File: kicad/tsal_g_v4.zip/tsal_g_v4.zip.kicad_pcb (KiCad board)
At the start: 2 copper layers, 115 x 60 mm, 92 parts, among them J1 Conn_01x02_Pin, J2 Conn_01x02_Pin, J3 Conn_01x06_Pin, J6 Conn_01x02_Pin, J7 Conn_01x02_Pin, J8 Conn_01x03, Q1 2N7002, Q2 NCE60P04R, U1 TL431DBZ, U10 BU4S01G2, U11 BU4S01G2, U14 BUS4S71G2, U15 BUS4S71G2, U16 BU4SU69G2, U17 40106, U18 BU4S01G2, U19 BU4S01G2, U2 LTV-817S, U20 4071, U3 B1212, U4 BU4SU69G2, U5 40106, U6 40106, U7 BU4S81G2

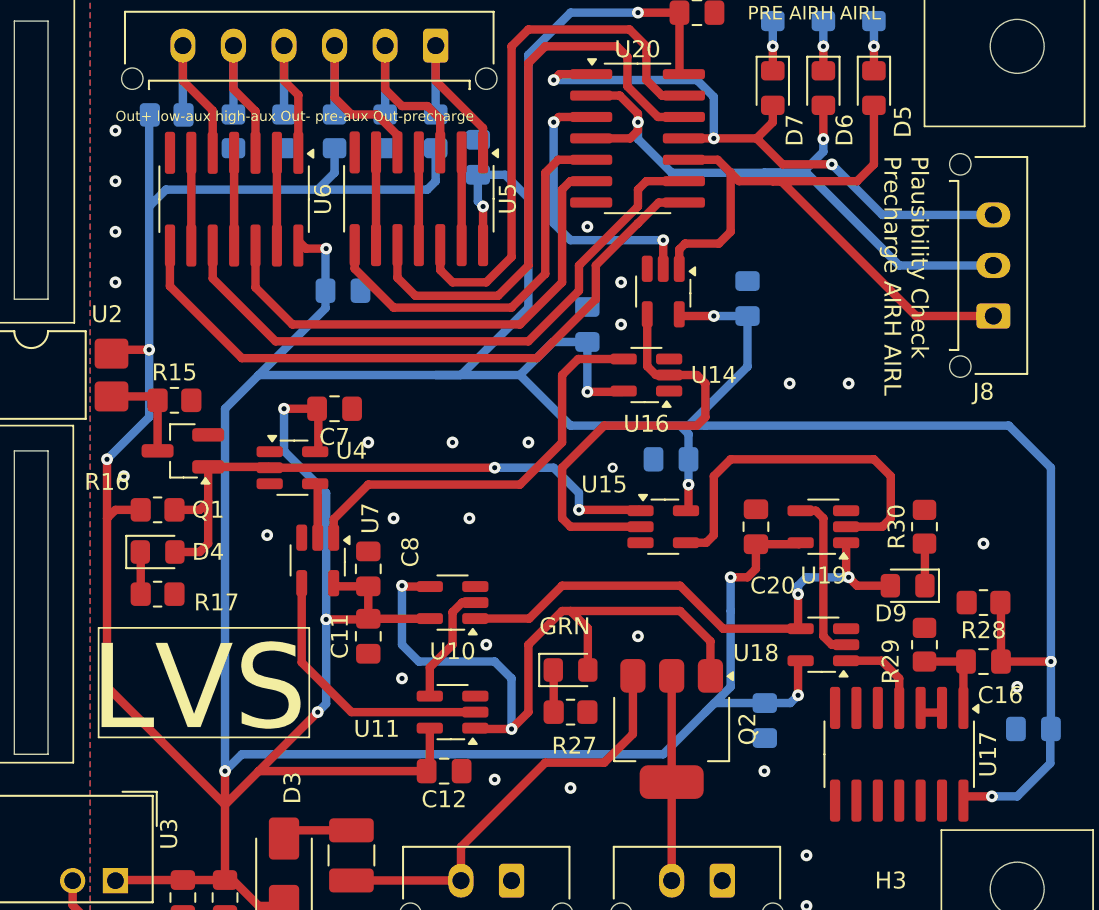
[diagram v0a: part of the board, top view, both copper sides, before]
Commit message: changed tsal_g traces
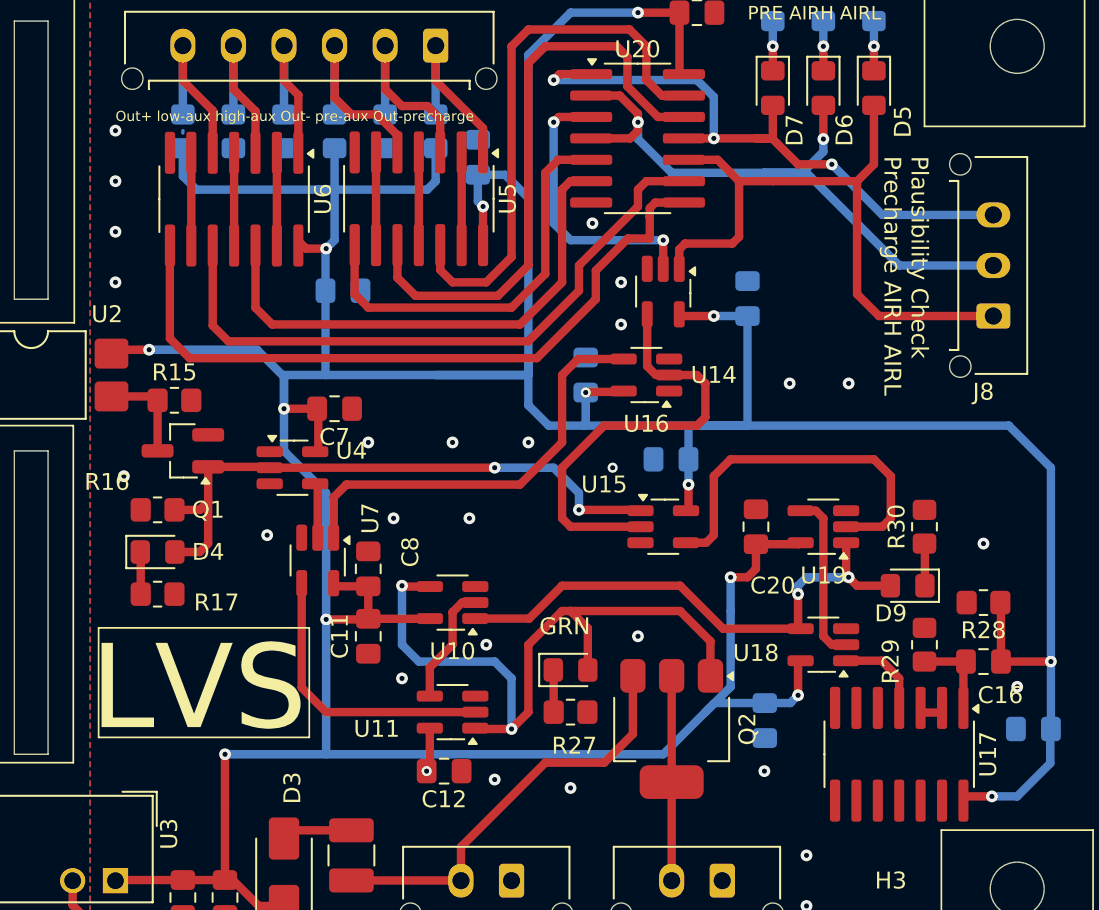
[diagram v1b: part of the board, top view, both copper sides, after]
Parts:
- moved C18 3.00 mm to (140.9, 77.5)
- moved R22 1.37 mm to (117.0, 63.0), turned to -90 degrees
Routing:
- net VCC: track 381.1 -> 309.9 mm, vias 16 -> 15
- net Out +: track 39.7 -> 42.4 mm
- net low aux: track 36.9 -> 38.5 mm
- net AIRL Check: track 40.5 -> 39.6 mm
- net Out -: track 24.1 -> 25.0 mm
- net Net-(U11-Pad2): track 16.2 -> 17.1 mm
- net RELAY LOGIC: track 24.6 -> 25.3 mm
- net high aux: track 30.6 -> 31.3 mm
- net Precharge Check: track 37.9 -> 38.5 mm

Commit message: updated tsal
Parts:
- removed C20: 0.1uF, Capacitor_SMD:C_0805_2012Metric_Pad1.18x1.45mm_HandSolder
- removed D8: LED, LED_SMD:LED_0805_2012Metric_Pad1.15x1.40mm_HandSolder
- removed Q2: NCE60P04R, Package_TO_SOT_SMD:SOT-223-3_TabPin2
- removed R27: 1k, Resistor_SMD:R_0805_2012Metric_Pad1.20x1.40mm_HandSolder
- removed U15: BUS4S71G2, Package_TO_SOT_SMD:SOT-23-5_HandSoldering
- removed U17: 40106, to be sorted:SOIC-14_3.9x8.7mm_P1.27mm_extendedpad
- removed U18, U19: BU4S01G2, Package_TO_SOT_SMD:SOT-23-5_HandSoldering
- added D10: LED, RMC_LED:LED_0805_2012Metric_Pad1.45x1.40mm_HandSolder, F.Cu at (168.4, 82.3)
- added Q4: QM6015D, RMC_TO:TO-252-2, F.Cu at (162.4, 85.0)
- added R31: 1k, RMC_Resistor:R_0805_2012Metric_Pad1.20x1.40mm_HandSolder_L, F.Cu at (168.4, 87.1)
- added U12: 4077, RMC_SO:SOIC127P600X175-14N, F.Cu at (144.4, 89.4)
- added U13: BU4S71G2, RMC_SOT:SOT-23-5_HandSoldering_Extended_RMC, F.Cu at (144.3, 82.5)
- added U9: 40106, RMC_SO:SOIC127P600X175-14N, F.Cu at (135.1, 89.3)
- C1, C11, C12, C16, C2, C24, C3, C4, C5, C6, C7, C8, C9: footprint Capacitor_SMD:C_0805_2012Metric_Pad1.18x1.45mm_HandSolder -> RMC_Capacitor:C_0805_2012Metric_Pad1.18x1.45mm_HandSolder_L
- C15, C17, C18, C19, C21, C22, C23: footprint Capacitor_SMD:C_0805_2012Metric_Pad1.18x1.45mm_HandSolder -> RMC_Capacitor:C_0805_2012Metric_Pad1.18x1.45mm_HandSolder_L; moved to F.Cu
- D2, D4, D5, D6, D7, D9: footprint LED_SMD:LED_0805_2012Metric_Pad1.15x1.40mm_HandSolder -> RMC_LED:LED_0805_2012Metric_Pad1.45x1.40mm_HandSolder
- D3: footprint Diode_SMD:D_SMA -> Diode_SMD:D_SMA_Handsoldering
- F2: footprint Fuse:Fuse_1210_3225Metric_Pad1.42x2.65mm_HandSolder -> to be sorted:Fuse_1210_3225Metric_Pad1.42x2.65mm_HandSolder
- LM1: footprint Package_SO:SOIC-8_3.9x4.9mm_P1.27mm -> RMC_SO:SOIC-8_3.9x4.9mm_P1.27mm_RMC_Handsolder
- Q1, U1: footprint Package_TO_SOT_SMD:SOT-23_Handsoldering -> RMC_SOT:SOT-23
- R1, R10, R11, R12, R13, R14, R15, R16, R17, R2, R28, R29, R3, R30, R4, R5, R6, R7, R8, R9: footprint Resistor_SMD:R_0805_2012Metric_Pad1.20x1.40mm_HandSolder -> RMC_Resistor:R_0805_2012Metric_Pad1.20x1.40mm_HandSolder_L
- R18, R19, R20, R21, R22, R23, R24, R25, R26: footprint Resistor_SMD:R_0805_2012Metric_Pad1.20x1.40mm_HandSolder -> RMC_Resistor:R_0805_2012Metric_Pad1.20x1.40mm_HandSolder_L; moved to F.Cu
- U10, U11, U14, U16, U7: footprint Package_TO_SOT_SMD:SOT-23-5_HandSoldering -> RMC_SOT:SOT-23-5_HandSoldering_Extended_RMC
- U20, U5, U6: footprint to be sorted:SOIC-14_3.9x8.7mm_P1.27mm_extendedpad -> RMC_SO:SOIC127P600X175-14N
- moved C11 40.1 mm to (167.3, 101.2), turned to 180 degrees
- moved U10 35.7 mm to (168.0, 98.0)
- moved C23 33.7 mm to (137.3, 83.5), turned to 180 degrees
- moved C16 33.6 mm to (132.8, 83.5)
- moved R29 30.8 mm to (132.7, 81.3), turned to 0 degrees
- moved U7 29.9 mm to (153.4, 98.0), turned to 0 degrees
- moved C12 29.8 mm to (161.6, 94.8), turned to 0 degrees
- moved R28 28.9 mm to (137.3, 81.3), turned to 0 degrees
- moved U11 27.8 mm to (160.8, 98.0), turned to 0 degrees
- moved C8 26.8 mm to (154.1, 94.8), turned to 0 degrees
- moved J8 25.0 mm to (147.4, 56.3), turned to 0 degrees
- moved C18 20.2 mm to (161.0, 75.6), turned to 180 degrees
- moved C19 19.7 mm to (145.0, 79.4), turned to 180 degrees
- moved U16 18.0 mm to (161.8, 72.4), turned to 0 degrees
- moved D9 17.9 mm to (142.8, 95.2)
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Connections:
- C19 pad 1: GLV- -> VCC
- C19 pad 2: VCC -> GLV-
- U16 pad 3: GLV- -> VCC
- U16 pad 5: VCC -> GLV-
- U20 pad 1: Precharge Check -> Out -
- U20 pad 10: AIRL Check -> Net-(U14-Pad2)
- U20 pad 11: Precharge Check -> AIRL Check
- U20 pad 12: pre aux -> Out +
- U20 pad 13: Out Precharge -> low aux
- U20 pad 2: AIRH Check -> high aux
- U20 pad 3: Net-(U14-Pad2) -> AIRH Check
- U20 pad 4: AIRH Check -> Precharge Check
- U20 pad 5: Out - -> pre aux
- U20 pad 6: high aux -> Out Precharge
- U20 pad 8: Out + -> Precharge Check
- U20 pad 9: low aux -> AIRH Check
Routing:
- net VCC: track 309.9 -> 11.8 mm, vias 15 -> 0
- net AIRL Check: track 39.6 -> 4.34 mm
- net Net-(Q4-G): track 41.4 -> 7.88 mm, vias 2 -> 0
- net RESET: track 31.8 -> 0.00 mm, vias 2 -> 0
- net AIRH Check: track 38.6 -> 8.05 mm, vias 2 -> 0
- net Precharge Check: track 38.5 -> 8.28 mm, vias 3 -> 0
- net TS RESET: track 36.3 -> 6.98 mm, vias 2 -> 0
- net RELAY LOGIC: track 25.3 -> 0.00 mm
- net GLV+: track 24.9 -> 0.00 mm
- net RELAY RESET: track 26.6 -> 3.97 mm
- net Net-(U15-Pad4): track 22.0 -> 0.00 mm
- net Out Precharge: track 32.6 -> 14.2 mm, vias 0 -> 2
- net pre aux: track 35.3 -> 18.8 mm, vias 0 -> 2
- net Net-(U14-Pad2): track 17.2 -> 4.20 mm, vias 2 -> 0
- net Net-(U11-Pad2): track 17.1 -> 4.53 mm
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
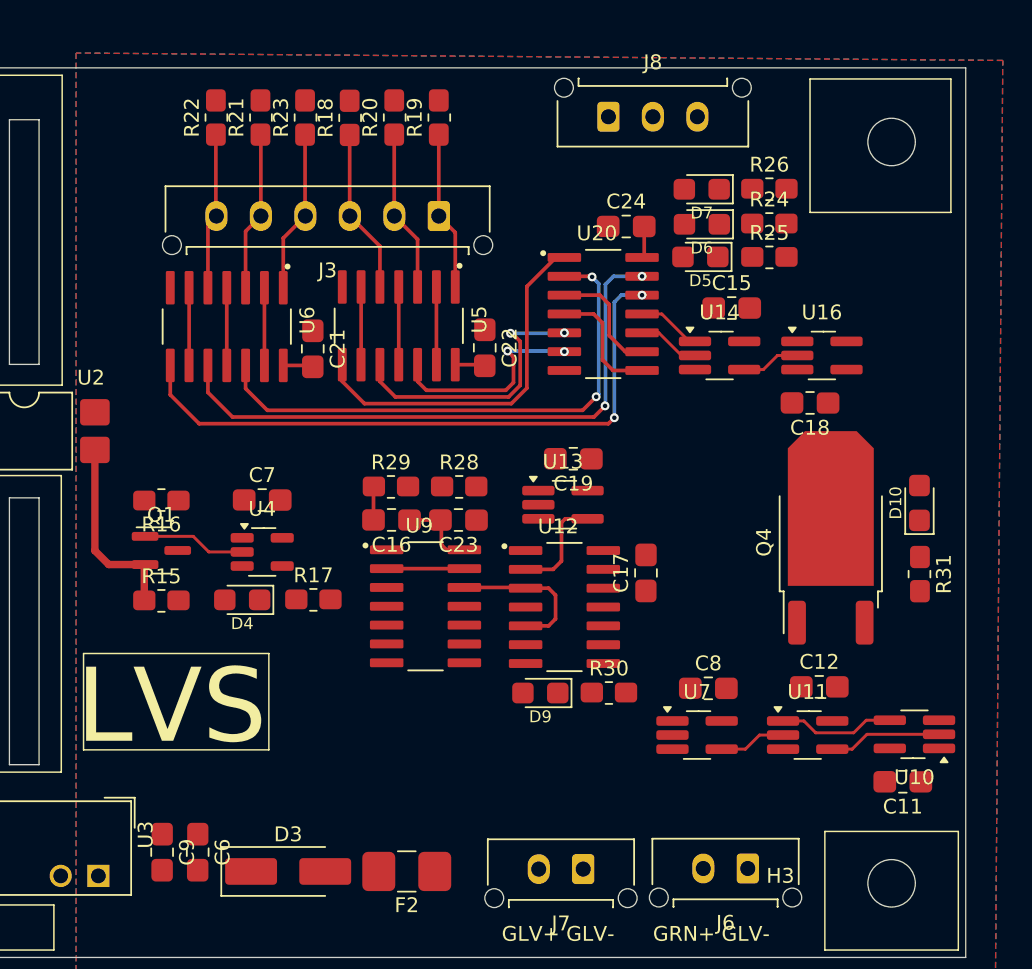
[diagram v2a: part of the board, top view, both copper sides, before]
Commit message: updated layout of tsal, need final touhces
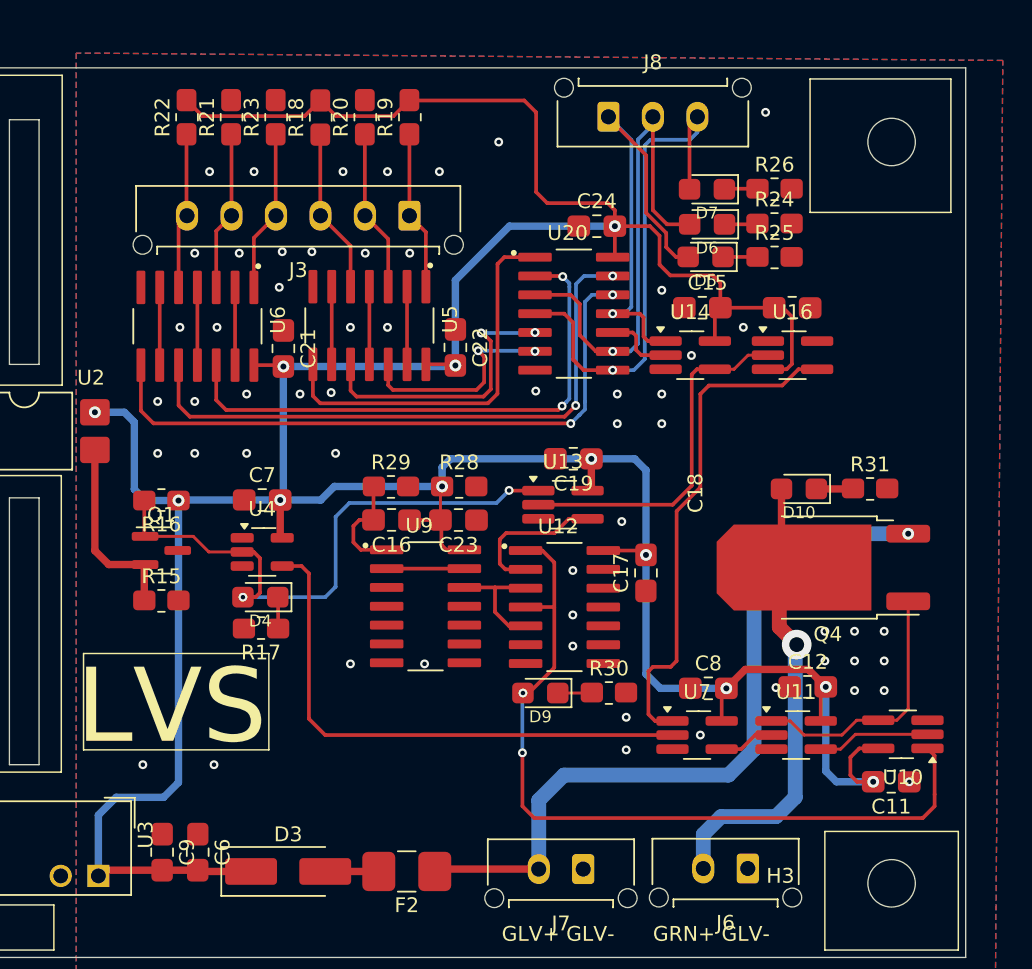
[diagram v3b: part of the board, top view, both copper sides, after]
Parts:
- moved D10 8.18 mm to (160.2, 81.4), turned to 180 degrees
- moved R31 6.64 mm to (165.1, 81.4), turned to 0 degrees
- moved C18 6.53 mm to (159.8, 69.2)
- moved R17 4.01 mm to (124.0, 90.8), turned to 180 degrees
- moved C22 1.98 mm to (137.1, 71.9)
- moved J3 1.98 mm to (134.0, 63.0)
- moved R19 1.98 mm to (134.0, 56.3)
- moved R20 1.98 mm to (131.0, 56.3)
- moved U14 1.98 mm to (152.9, 72.4)
- moved U16 1.98 mm to (159.8, 72.4)
- moved U20 1.98 mm to (145.1, 69.6)
- moved R21 1.98 mm to (122.0, 56.3)
- moved R22 1.98 mm to (119.0, 56.3)
- moved R23 1.98 mm to (125.0, 56.3)
- moved U6 1.98 mm to (119.7, 70.4)
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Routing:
- net VCC: track 11.8 -> 253.4 mm, vias 0 -> 12
- net RESET: track 0.00 -> 54.3 mm, vias 0 -> 2
- net GLV+: track 0.00 -> 51.8 mm, vias 0 -> 1
- net TS LOGIC: track 0.00 -> 36.8 mm
- net RELAY LOGIC: track 0.00 -> 34.1 mm
- net TS RESET: track 6.98 -> 40.1 mm, vias 0 -> 2
- net /GRN+: track 0.00 -> 31.6 mm, vias 0 -> 1
- net AIRL Check: track 4.34 -> 32.2 mm, vias 0 -> 1
- net Precharge Check: track 8.28 -> 35.2 mm, vias 0 -> 1
- net AIRH Check: track 8.05 -> 34.9 mm, vias 0 -> 1
- net RELAY RESET: track 3.97 -> 24.1 mm
- net Net-(Q4-G): track 7.88 -> 17.6 mm
- net Net-(C16-Pad2): track 2.27 -> 7.35 mm
- net Net-(D3-A): track 0.00 -> 3.61 mm
- net Net-(U12-Pad2): track 7.12 -> 10.0 mm
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
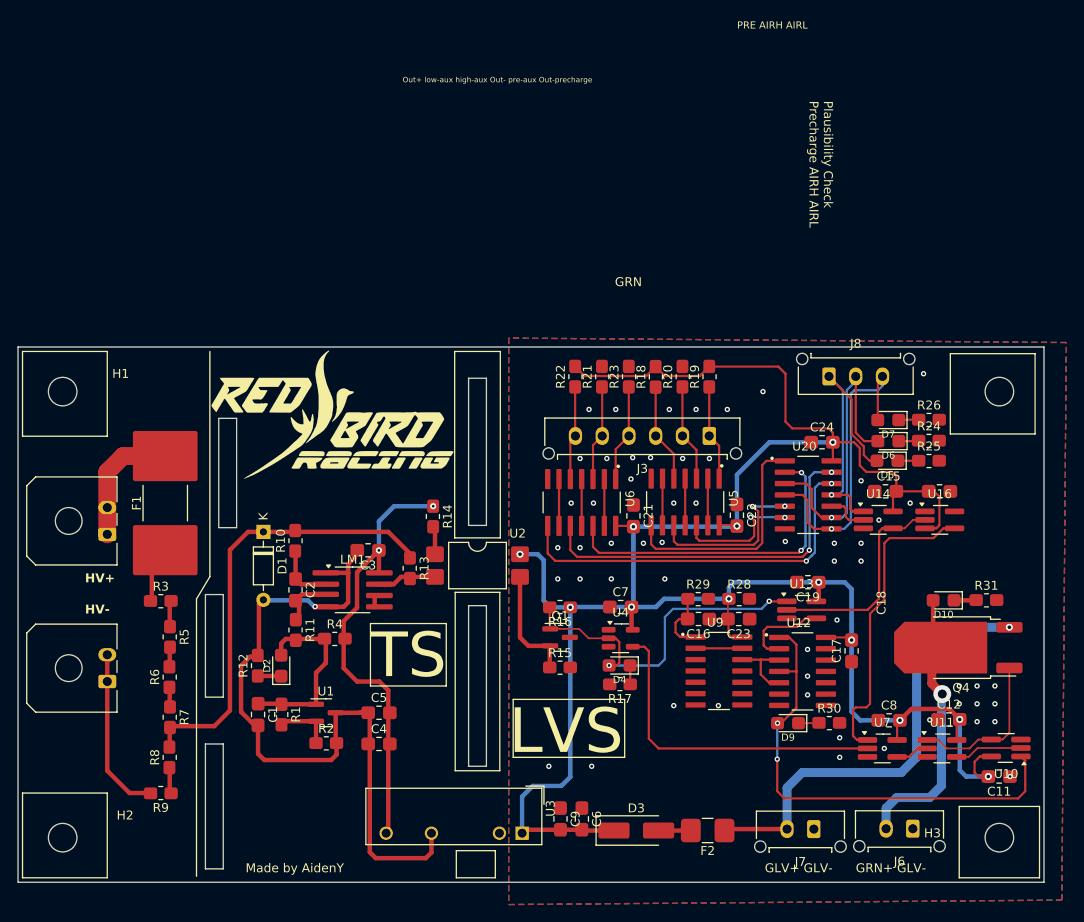
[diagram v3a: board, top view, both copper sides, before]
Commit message: Plausibility check and ERC debug
-inverted plausibility check pin out
-arrange silkscreen reference
-debug ERC
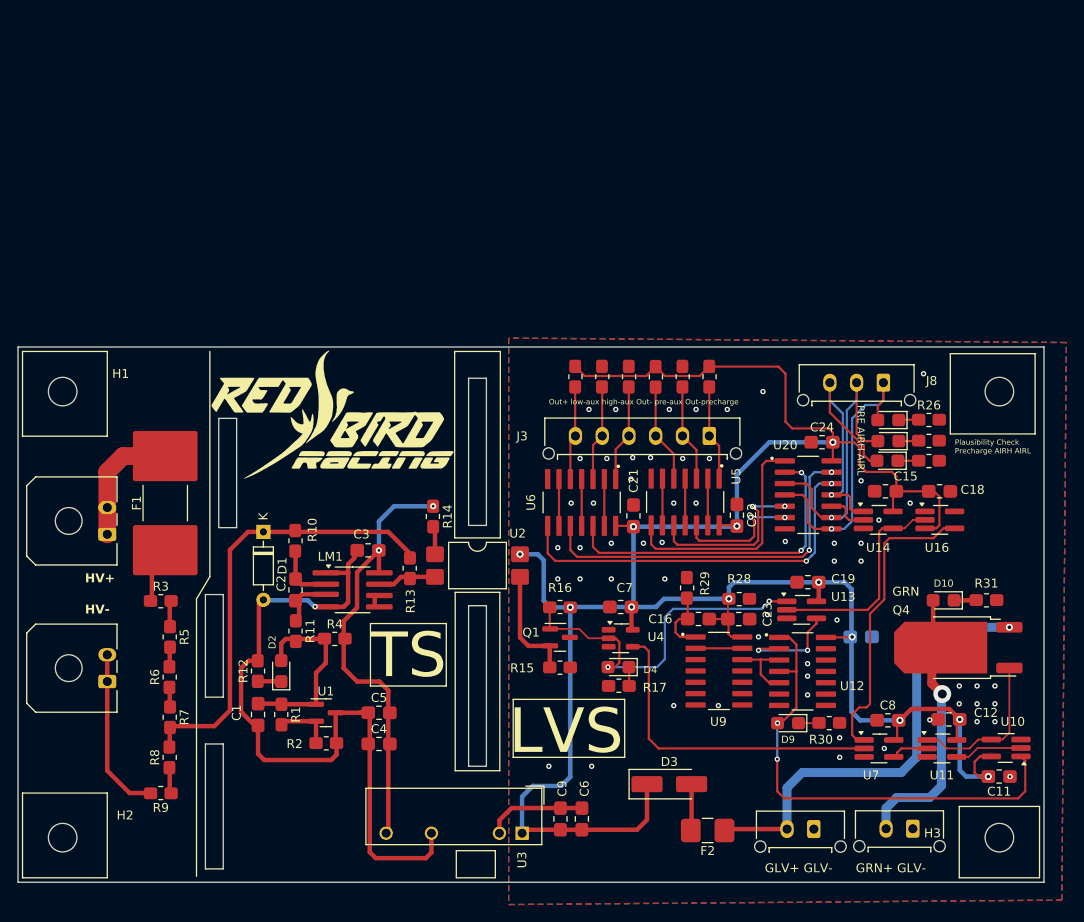
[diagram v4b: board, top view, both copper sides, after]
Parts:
- C17: moved to B.Cu
- moved D3 6.38 mm to (129.5, 102.0)
- moved J8 6.14 mm to (153.5, 57.0), turned to 180 degrees
- moved C17 1.89 mm to (151.0, 85.5), turned to 180 degrees
- moved R29 1.77 mm to (131.5, 80.0), turned to 90 degrees
- moved D2 0.60 mm to (86.0, 89.3)
- moved R12 0.60 mm to (83.4, 89.3)
- moved U7 0.38 mm to (153.0, 98.0)
- moved R17 0.22 mm to (123.8, 91.0)
- moved D4 0.22 mm to (123.8, 88.9)
- moved C8 0.14 mm to (154.0, 94.8)
- moved R11 0.12 mm to (87.6, 84.8)
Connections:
- J8 pad 1: AIRL Check -> Precharge Check
- J8 pad 3: Precharge Check -> AIRL Check
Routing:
- net GLV-: track 0.00 -> 11.3 mm, vias 56 -> 58
- net VCC: track 253.4 -> 261.6 mm
- net Net-(U12-Pad2): track 10.0 -> 11.9 mm, vias 0 -> 2
- net Net-(D3-A): track 3.61 -> 5.24 mm
- net AIRL Check: track 32.2 -> 30.7 mm
- net AIRH Check: track 34.9 -> 34.0 mm
- net Precharge Check: track 35.2 -> 35.9 mm
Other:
- board text removed: "Made by AidenY"

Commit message: TSAL_G final touches
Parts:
- removed the G*** at (92.0, 60.5)
- added G***: LOGO, LOGO, F.Cu at (93.0, 62.0)
- C17: moved to F.Cu
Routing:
- net Net-(F1-Pad1): track 6.35 -> 12.7 mm
- net GLV-: track 11.3 -> 16.8 mm, vias 58 -> 78
- net /Vin: track 50.5 -> 53.7 mm
- net Net-(R8-Pad1): track 3.00 -> 5.96 mm
- net /-HV: track 19.0 -> 21.4 mm
- net Net-(R6-Pad1): track 2.50 -> 4.72 mm
- net Net-(R5-Pad2): track 2.50 -> 4.72 mm
- net VCC: track 261.6 -> 260.5 mm
- net RELAY LOGIC: track 34.0 -> 35.0 mm
- net AIRL Check: track 30.7 -> 31.7 mm
- net +12V: track 49.5 -> 50.3 mm
- net Precharge Check: track 35.9 -> 36.4 mm
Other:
- outline, holes or cut-outs redrawn
- board text added: "TSAL_G_v2 AidenY 11/07/2025"
